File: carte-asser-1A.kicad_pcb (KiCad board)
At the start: 2 copper layers, 56 parts, among them K1 Maxon-200142, K2 Maxon-200142, P1 swdio, P2 CAN bus, P3 USB_OTG, P4 serial bus, P5 5V, P6 8..24V, Q1 Q_PNP_BCE, Q2 Q_PNP_BCE, U2 DEC24/2, U3 DEC24/2, U4 stm32f042k6tx, U5 MCP2562, U7 USBLC6-2, U8 MC7805CDTG

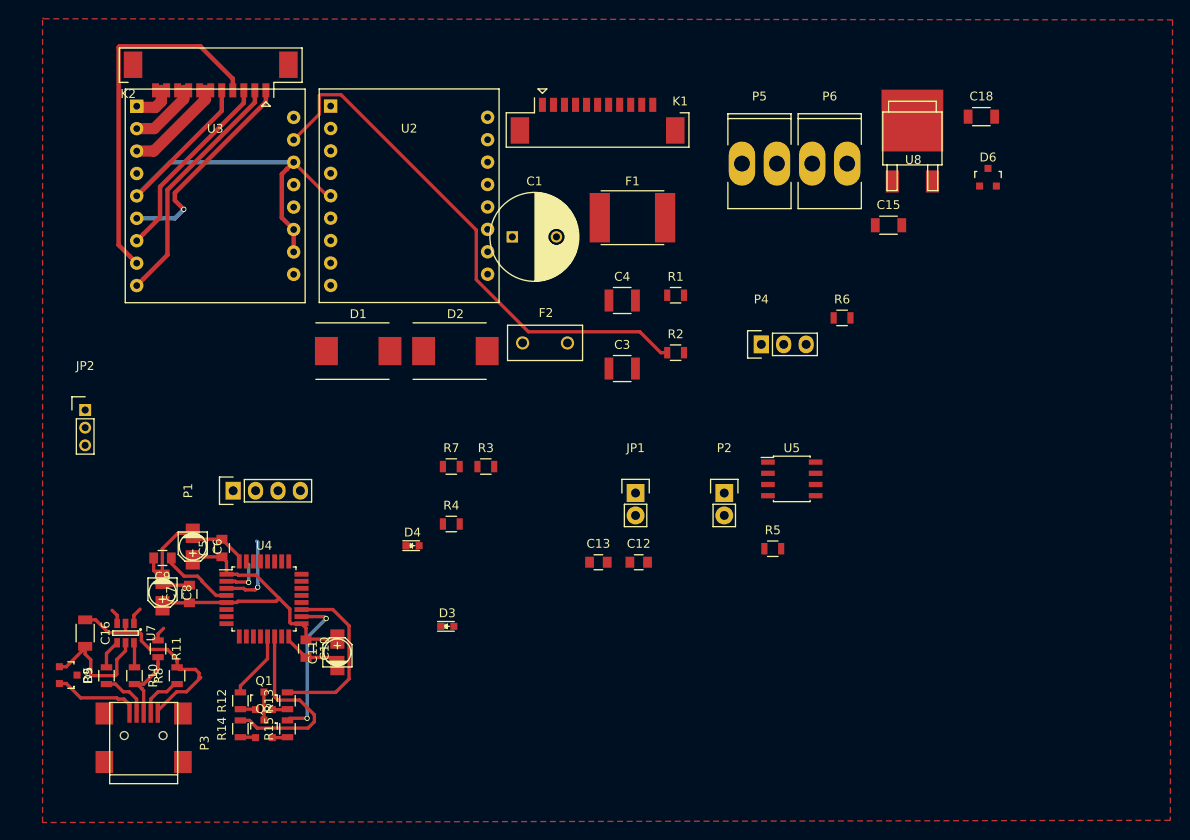
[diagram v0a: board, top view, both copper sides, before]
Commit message: schematic seems ok, ongoing routing
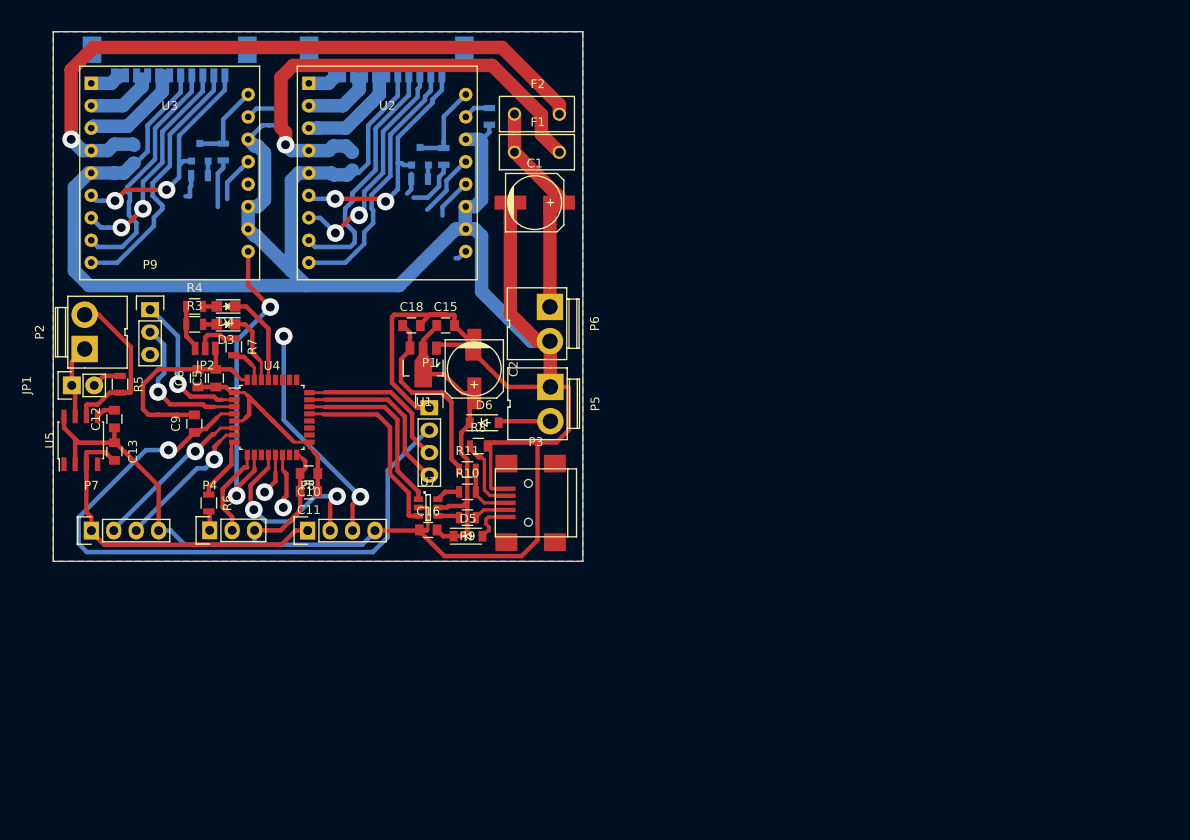
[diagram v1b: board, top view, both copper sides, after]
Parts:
- removed C7: 10n, Capacitors_SMD:C_0805
- removed C8: 1u, Capacitors_SMD:c_elec_3x5.3
- removed U8: MC7805CDTG, TO_SOT_Packages_SMD:SOT-428
- added C2: 100u, Capacitors_SMD:c_elec_6.3x4.5, F.Cu at (72.5, 66.1)
- added P7: encoder 1, Socket_Strips:Socket_Strip_Straight_1x04, F.Cu at (29.1, 84.4)
- added P8: encoder 2, Socket_Strips:Socket_Strip_Straight_1x04, F.Cu at (53.7, 84.4)
- added P9: i2c bus, Pin_Headers:Pin_Header_Straight_1x03, F.Cu at (35.8, 59.4)
- added U1: MCP1702, TO_SOT_Packages_SMD:SOT89-3_Housing, F.Cu at (66.7, 65.6)
- C1: value 100u/35v -> 100u/35v EEEHA1V101XP; footprint Capacitors_ThroughHole:C_Radial_D10_L13_P5 -> Capacitors_SMD:c_elec_6.3x4.5
- C11, C6: footprint Capacitors_SMD:c_elec_3x5.3 -> Capacitors_SMD:C_0805
- C15, C18: value 330n -> 1u; footprint Capacitors_SMD:C_1206 -> Capacitors_SMD:C_0805
- C16: footprint Capacitors_SMD:C_1206 -> Capacitors_SMD:C_0805
- C3, C4: footprint Capacitors_SMD:C_1210 -> Capacitors_SMD:C_0805; moved to B.Cu
- D1, D2: value Schottky/26V -> Schottky/26V MBR0530T1G; footprint Diodes_SMD:DO-214AB -> Diodes_SMD:SOD-123; moved to B.Cu
- D3, D4: footprint LEDs:LED_0603 -> LEDs:LED_0805
- D5, D6: value D_Small -> MBR0530T1G; footprint TO_SOT_Packages_SMD:SOT-23 -> Diodes_SMD:SOD-123
- F1: value FUSE/3A -> FUSE/3A MF-R300; footprint Fuse_Holders_and_Fuses:Fuse_SMD2920 -> Fuse_Holders_and_Fuses:Fuse_TE5_Littlefuse-395Series
- F2: value FUSE/3A -> FUSE/3A MF-R300
- JP2: value JUMPER3 -> boot mode; footprint Pin_Headers:Pin_Header_Straight_1x03_Pitch2.00mm -> de24-2:jumper_switch_3
- K1, K2, R1, R12, R14, R2: moved to B.Cu
- P2: footprint Pin_Headers:Pin_Header_Straight_1x02 -> Connect:JWT_Vertical_A3963-RM3.96mm-2
- P3: value USB_OTG -> usb
- P5, P6: footprint Sockets_MOLEX_KK-System:Socket_MOLEX-KK-RM3-96mm_Lock_2pin_straight -> Connect:JWT_Vertical_A3963-RM3.96mm-2
- Q1, Q2: value Q_PNP_BCE -> BC807; moved to B.Cu
- R13, R15: value 100 -> 1k; moved to B.Cu
- U4: footprint Housings_QFP:TQFP-32_7x7mm_Pitch0.8mm -> Housings_QFP:LQFP-32_7x7mm_Pitch0.8mm
- moved U5 80.7 mm to (28.0, 74.2), turned to 90 degrees
- moved R5 76.3 mm to (32.4, 67.8), turned to 270 degrees
- moved R6 74.7 mm to (42.5, 81.3), turned to 270 degrees
- moved P2 74.3 mm to (28.4, 63.8), turned to 90 degrees
- moved C18 68.8 mm to (65.4, 61.2)
- moved P4 65.9 mm to (42.6, 84.4)
- moved R15 65.7 mm to (44.1, 41.5), turned to 270 degrees
- moved Q2 65.7 mm to (41.4, 41.5), turned to 180 degrees
- moved JP1 65.0 mm to (26.9, 68.0), turned to 90 degrees
- moved Q1 64.2 mm to (66.4, 42.0), turned to 180 degrees
- moved R13 64.2 mm to (69.1, 42.0), turned to 270 degrees
- moved D6 63.5 mm to (73.6, 72.2)
- moved R14 62.8 mm to (41.4, 44.2), turned to 0 degrees
- moved R12 62.5 mm to (66.3, 44.6), turned to 0 degrees
- moved C12 61.6 mm to (31.8, 71.8), turned to 90 degrees
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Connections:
- net Net-(C3-Pad1) renamed /brushless-part/power1
- net Net-(C4-Pad1) renamed /brushless-part/power2
- K1 pad 1: +5V_weak -> /brushless-part/W1_1
- K1 pad 11: Net-(K1-Pad10) -> +5V_weak1
- K1 pad 2: Net-(K1-Pad2) -> /brushless-part/W1_1
- K1 pad 3: Net-(K1-Pad3) -> /brushless-part/W1_2
- K1 pad 4: Net-(K1-Pad4) -> /brushless-part/W1_2
- K1 pad 5: GND -> /brushless-part/W1_3
- K1 pad 6: Net-(K1-Pad6) -> /brushless-part/W1_3
- K1 pad 7: Net-(K1-Pad6) -> GND
- K1 pad 9: Net-(K1-Pad8) -> Net-(K1-Pad9)
- K2 pad 1: Net-(K2-Pad1) -> /brushless-part/W2_1
- K2 pad 11: Net-(K2-Pad10) -> +5V_weak2
- K2 pad 2: Net-(K2-Pad2) -> /brushless-part/W2_1
- K2 pad 3: Net-(K2-Pad3) -> /brushless-part/W2_2
- K2 pad 4: Net-(K2-Pad4) -> /brushless-part/W2_2
- K2 pad 5: GND -> /brushless-part/W2_3
- K2 pad 6: Net-(K2-Pad6) -> /brushless-part/W2_3
- K2 pad 7: Net-(K2-Pad6) -> GND
- K2 pad 9: Net-(K2-Pad8) -> Net-(K2-Pad9)
- P4 pad 1: /serial-part/rx -> Net-(P4-Pad1)
- P4 pad 2: /serial-part/rx -> /serial-part/tx
- P6 pad 1: GND -> +24V
- P6 pad 2: +24V -> GND
- Q1 pad 2: /brushless-part/motor1_speed -> +5V_weak1
- Q1 pad 3: +5V_weak -> /brushless-part/motor1_speed
- Q2 pad 2: /brushless-part/motor2_speed -> +5V_weak2
- Q2 pad 3: +5V_weak -> /brushless-part/motor2_speed
- R12 pad 1: Net-(Q1-Pad1) -> /uC-part/pwm1_neg
- R12 pad 2: /uC-part/pwm1_neg -> Net-(Q1-Pad1)
- R14 pad 1: Net-(Q2-Pad1) -> /uC-part/pwm2_neg
- R14 pad 2: /uC-part/pwm2_neg -> Net-(Q2-Pad1)
- R6 pad 2: /serial-part/rx -> Net-(P4-Pad1)
- U2 pad 1: Net-(K1-Pad10) -> /brushless-part/W1_1
- U2 pad 2: Net-(K1-Pad8) -> /brushless-part/W1_2
- U2 pad 3: Net-(K1-Pad6) -> /brushless-part/W1_3
- U2 pad 6: +5V_weak -> +5V_weak1
- U2 pad 7: Net-(K1-Pad3) -> Net-(K1-Pad9)
- U2 pad 8: Net-(K1-Pad4) -> Net-(K1-Pad8)
- U2 pad 9: Net-(K1-Pad2) -> Net-(K1-Pad10)
- U3 pad 1: Net-(K2-Pad10) -> /brushless-part/W2_1
- U3 pad 2: Net-(K2-Pad8) -> /brushless-part/W2_2
- U3 pad 3: Net-(K2-Pad6) -> /brushless-part/W2_3
- U3 pad 6: Net-(K2-Pad1) -> +5V_weak2
- U3 pad 7: Net-(K2-Pad3) -> Net-(K2-Pad9)
- U3 pad 8: Net-(K2-Pad4) -> Net-(K2-Pad8)
- U3 pad 9: Net-(K2-Pad2) -> Net-(K2-Pad10)
- U4 pad 10: /uC-part/gpio_ready1 -> /uC-part/gpio_ready2
- U4 pad 11: /uC-part/gpio_ready2 -> Net-(U4-Pad11)
- U4 pad 12: /uC-part/tim3_ch1_encoder -> /encoder-part/encoder2_1
- U4 pad 15: /uC-part/gpio_direction1 -> Net-(U4-Pad15)
- U4 pad 25: Net-(U4-Pad25) -> /uC-part/gpio_direction1
- U4 pad 27: Net-(U4-Pad27) -> /uC-part/gpio_ready1
- U4 pad 28: /uC-part/tim3_ch2_encoder -> /encoder-part/encoder2_2
- U4 pad 6: /uC-part/tim2_ch1_encoder -> /encoder-part/encoder1_1
- U4 pad 7: /uC-part/tim2_ch2_encoder -> /encoder-part/encoder1_2
- U4 pad 9: /serial-part/rx -> /serial-part/tx
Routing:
- net GND: track 105.3 -> 400.8 mm
- net /brushless-part/power2: track 0.00 -> 76.0 mm, vias 0 -> 1
- net /uC-part/nrst: track 8.41 -> 76.2 mm, vias 0 -> 1
- net +5V: track 14.5 -> 72.7 mm
- net Net-(R2-Pad1): track 61.1 -> 3.97 mm
- net /brushless-part/power1: track 0.00 -> 53.7 mm, vias 0 -> 1
- net Net-(K2-Pad4): track 41.1 -> 0.00 mm
- net /uC-part/gpio_ready2: track 0.00 -> 35.8 mm, vias 0 -> 2
- net Net-(K1-Pad10): track 0.00 -> 29.6 mm
- net Net-(K1-Pad8): track 0.00 -> 28.2 mm
- net Net-(K2-Pad2): track 27.7 -> 0.00 mm
- net +5V_weak1: track 0.00 -> 27.6 mm, vias 0 -> 2
- net +5V_weak2: track 0.00 -> 26.6 mm, vias 0 -> 2
- net Net-(K1-Pad9): track 0.00 -> 26.0 mm, vias 0 -> 2
- net /encoder-part/encoder2_2: track 0.00 -> 26.0 mm, vias 0 -> 2
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- added copper zone on B.Cu, net GND
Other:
- board outline added: 60 x 60 mm
- net class Default: trace_width 0.381 -> 0.508; via_dia 0.6 -> 2; via_drill 0.4 -> 1
- net class fat added: clearance 0.508, trace_width 1.524, via_dia 2, via_drill 1
- net class normal removed
- net class power removed
- net class slim added: clearance 0.3302, trace_width 0.381, via_dia 2, via_drill 1
